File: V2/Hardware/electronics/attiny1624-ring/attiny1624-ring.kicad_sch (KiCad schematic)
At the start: 25 parts, among them J1 CHAIN_RING, J3 STEPPER_DRIVER_IN, J4 HOME_SENSOR, J5 UPDI_2X3, U1 ATtiny1624-SS

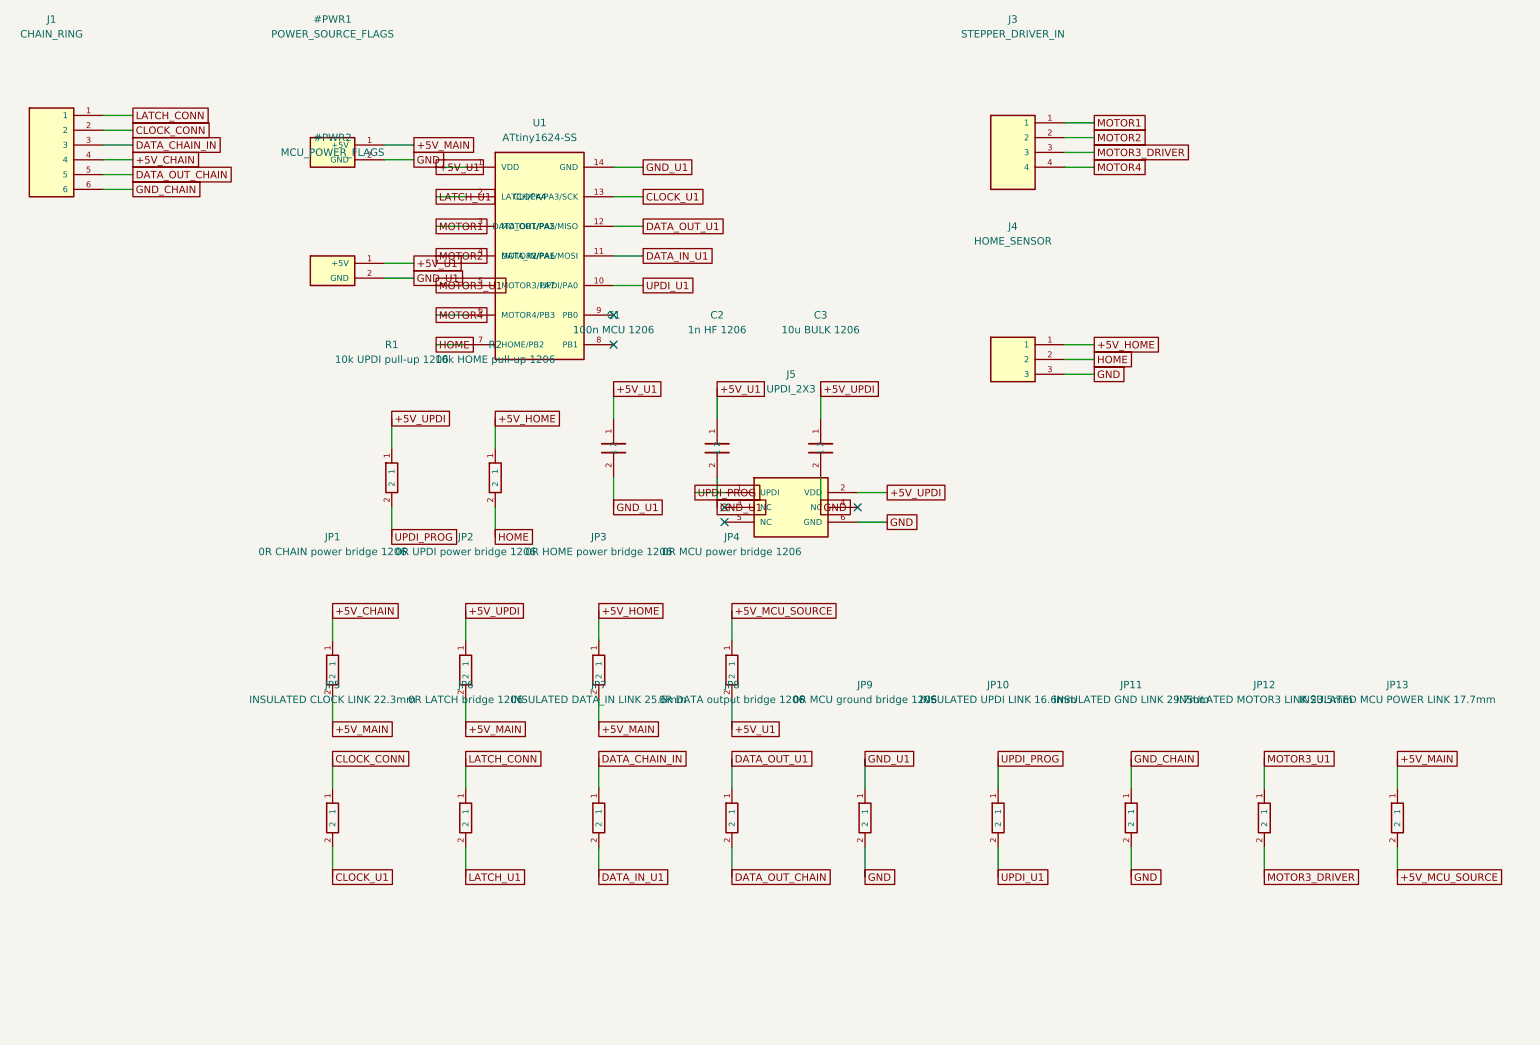
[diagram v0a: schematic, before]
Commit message: Align ATtiny1624 board with module firmware
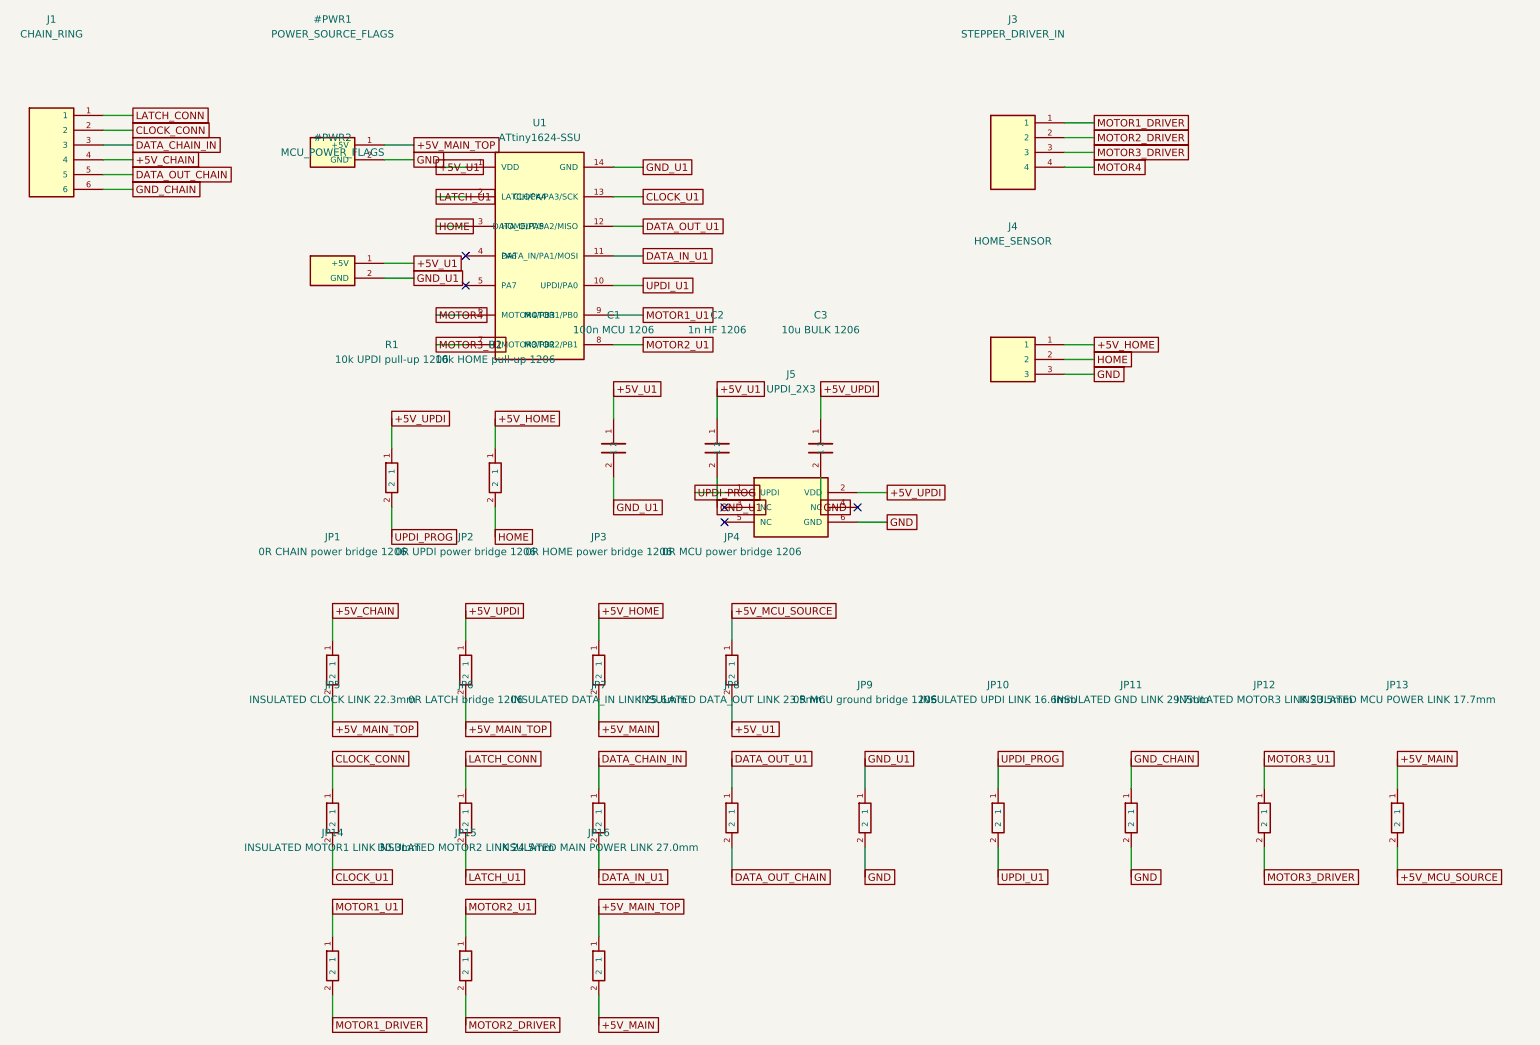
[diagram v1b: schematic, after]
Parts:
- added JP14: INSULATED MOTOR1 LINK 30.3mm, Alphabets:WireLink_30.3mm_SMD, symbol attiny1624-ring:R
- added JP15: INSULATED MOTOR2 LINK 24.5mm, Alphabets:WireLink_24.5mm_SMD, symbol attiny1624-ring:R
- added JP16: INSULATED MAIN POWER LINK 27.0mm, Alphabets:WireLink_27.0mm_SMD, symbol attiny1624-ring:R
- JP8: value 0R DATA output bridge 1206 -> INSULATED DATA_OUT LINK 23.5mm; footprint Resistor_SMD:R_1206_3216Metric_Pad1.30x1.75mm_HandSolder -> Alphabets:WireLink_23.5mm_SMD
- U1: value ATtiny1624-SS -> ATtiny1624-SSU
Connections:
- net +5V_MAIN: now also JP16.2; no longer #PWR1.1 (+5V), JP1.2, JP2.2
- net HOME: now also U1.3 (HOME/PA5); no longer U1.7 (HOME/PB2)
- net MOTOR3_U1: now also U1.7 (MOTOR3/PB2); no longer U1.5 (MOTOR3/PA7)
- net MOTOR2_U1: now reaches U1.8 (MOTOR2/PB1)
- net MOTOR2_U1: now also JP15.1
- net MOTOR1_U1: now reaches U1.9 (MOTOR1/PB0)
- net MOTOR1_U1: now also JP14.1
- net MOTOR1 renamed MOTOR1_DRIVER
- net MOTOR1_DRIVER: now also JP14.2; no longer U1.3 (MOTOR1/PA5)
- net MOTOR2: no longer names the net of U1.4 (PA6)
- net MOTOR2: no longer J3.2
- new net +5V_MAIN_TOP: #PWR1.1 (+5V), JP1.2, JP16.1, JP2.2
- new net MOTOR2_DRIVER: J3.2, JP15.2
